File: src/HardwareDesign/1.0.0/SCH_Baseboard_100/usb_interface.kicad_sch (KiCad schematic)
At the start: 1 part, among them J3 USB-TYPE-C-018

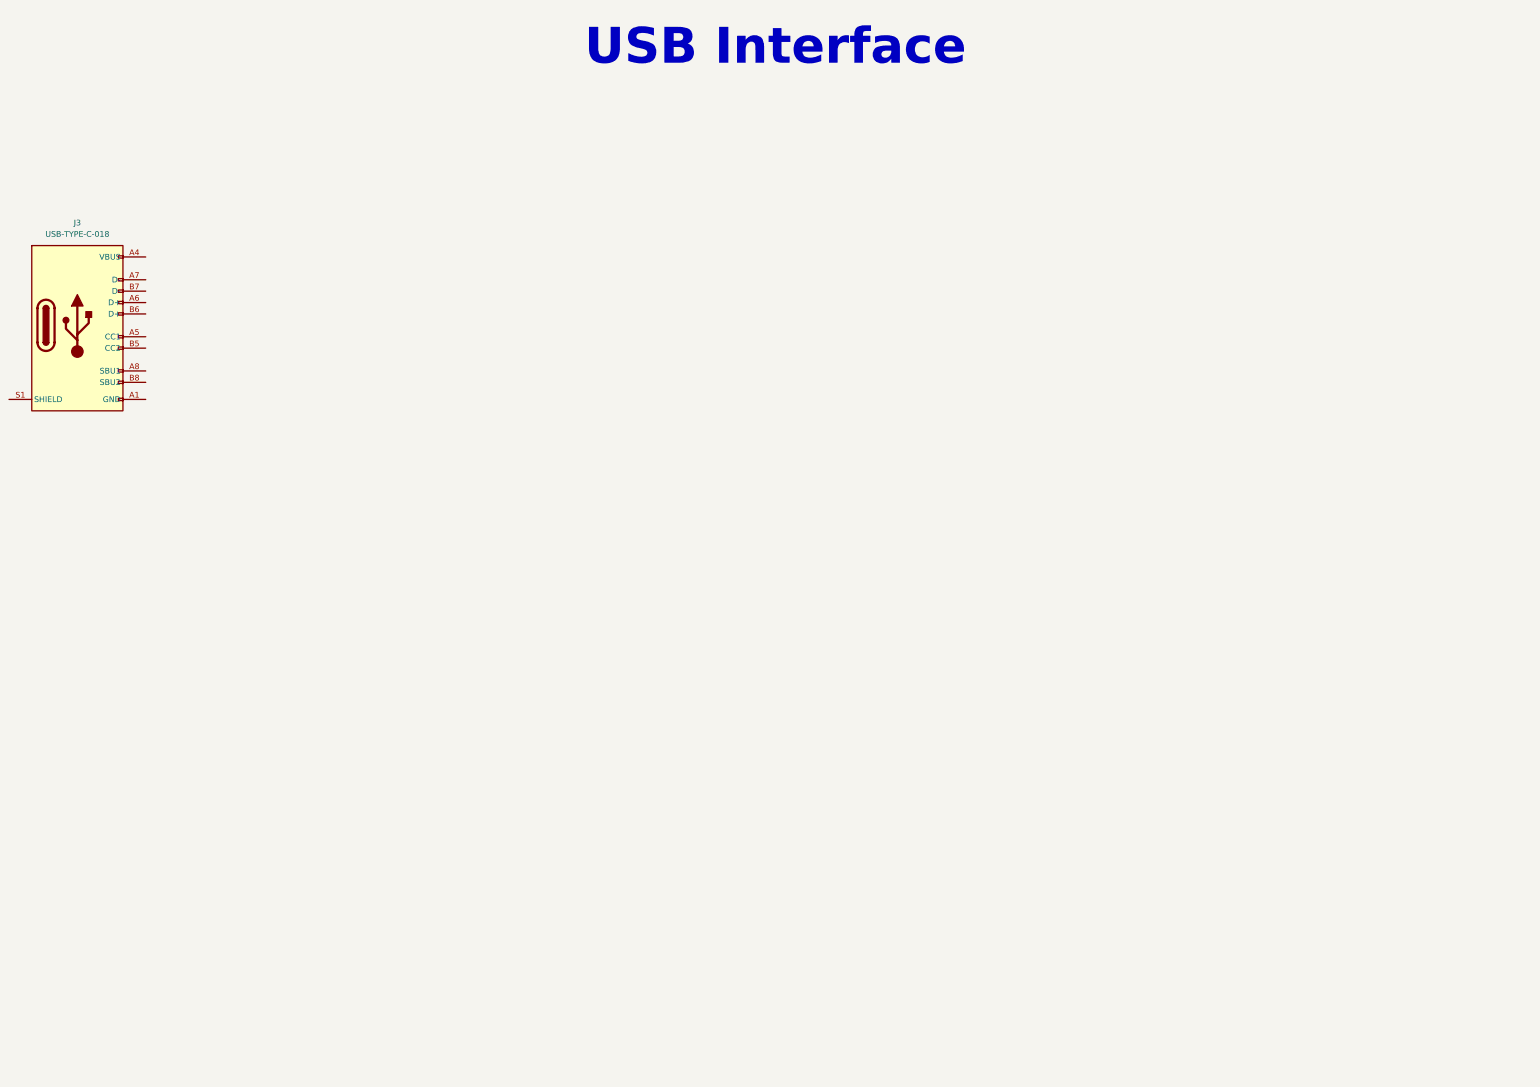
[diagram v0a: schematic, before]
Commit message: Add bladecore to design
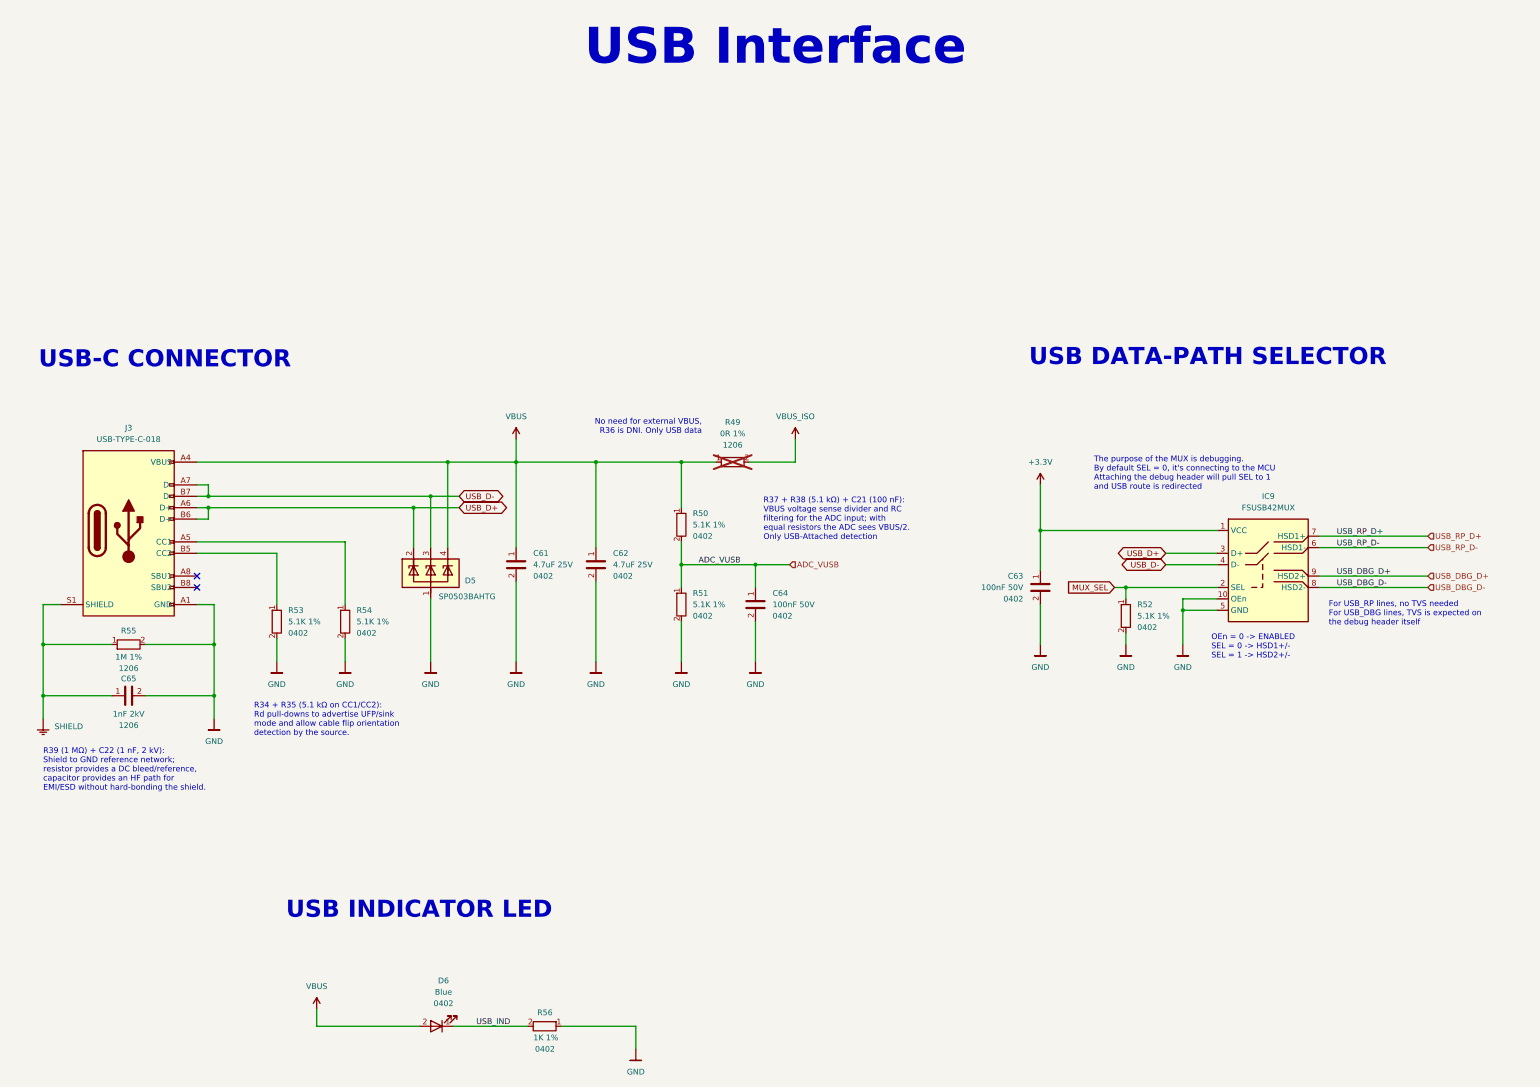
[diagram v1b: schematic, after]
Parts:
- added C61, C62: 4.7uF 25V, Capacitor_SMD:C_0402_1005Metric, symbol DS_Capacitor_0402:4.7uF 25V 0402
- added C63, C64: 100nF 50V, Capacitor_SMD:C_0402_1005Metric, symbol DS_Capacitor_0402:100nF 50V 0402
- added C65: 1nF 2kV, Capacitor_SMD:C_1206_3216Metric, symbol DS_Capacitor_1206:1nF 2kV 1206
- added D5: SP0503BAHTG, DS_Diode:SOT143, symbol DS_Diode:SP0503BAHTG
- added D6: Blue, LED_SMD:LED_0402_1005Metric, symbol DS_Opto:Blue 0402
- added IC9: FSUSB42MUX, DS_Peripherals:MSOP-10_3x3mm_P0.5mm, symbol DS_Peripherals:FSUSB42MUX
- added R49: 0R 1%, Resistor_SMD:R_1206_3216Metric, symbol DS_Resistor_1206:0R 1% 1206
- added R50, R51, R52, R53, R54: 5.1K 1%, Resistor_SMD:R_0402_1005Metric, symbol DS_Resistor_0402:5.1K 1% 0402
- added R55: 1M 1%, Resistor_SMD:R_1206_3216Metric, symbol DS_Resistor_1206:1M 1% 1206
- added R56: 1K 1%, Resistor_SMD:R_0402_1005Metric, symbol DS_Resistor_0402:1K 1% 0402
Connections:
- net GND: now reaches J3.A1 (GND), J3.A12 (GND), J3.B1 (GND), J3.B12 (GND)
- net GND: now also C61.2, C62.2, C63.2, C64.2, C65.2, D5.1, IC9.10 (OEn), IC9.5 (GND), R51.2, R52.2, R53.2, R54.2, R55.2, R56.1
- net VBUS: now reaches J3.A4 (VBUS), J3.A9 (VBUS), J3.B4 (VBUS), J3.B9 (VBUS)
- net VBUS: now also C61.1, C62.1, D5.4, D6.2, R49.1, R50.1
- net at J3.A5 (CC1): now also R54.1
- net USB_D+: now reaches J3.A6 (D+)
- net USB_D+: now also J3.B6 (D+), D5.2, IC9.3 (D+)
- net USB_D-: now reaches J3.A7 (D-)
- net USB_D-: now also J3.B7 (D-), D5.3, IC9.4 (D-)
- net at J3.B5 (CC2): now also R53.1
- net SHIELD: now reaches J3.S1 (SHIELD)
- net SHIELD: now also C65.1, R55.1
- new net +3.3V: C63.1, IC9.1 (VCC)
- new net ADC_VUSB: C64.1, R50.2, R51.1
- new net MUX_SEL: IC9.2 (SEL), R52.1
- new net USB_DBG_D+: IC9.9 (HSD2+)
- new net USB_DBG_D-: IC9.8 (HSD2-)
- new net USB_IND: D6.1, R56.2
- new net USB_RP_D+: IC9.7 (HSD1+)
- new net USB_RP_D-: IC9.6 (HSD1-)
- new net VBUS_ISO: R49.2
- no-connect marks 0 -> 2
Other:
- note added: "For USB_RP lines, no TVS needed For USB_DBG lines, TVS is expected on the debug header itself"
- note added: "No need for external VBUS, R36 is DNI. Only USB data"
- note added: "OEn = 0 -> ENABLED SEL = 0 -> HSD1+/- SEL = 1 -> HSD2+/-"
- note added: "R34 + R35 (5.1 kΩ on CC1/CC2): Rd pull-downs to advertise UFP/sink mode and allow cable flip orientation detection by the source."
- note added: "R37 + R38 (5.1 kΩ) + C21 (100 nF): VBUS voltage sense divider and RC filtering for the ADC input; with equal resistors the ADC sees VBUS/2. Only USB-Attached detection"
- note added: "R39 (1 MΩ) + C22 (1 nF, 2 kV): Shield to GND reference network; resistor provides a DC bleed/reference, capacitor provides an HF path for EMI/ESD without hard-bonding the shield."
- note added: "The purpose of the MUX is debugging. By default SEL = 0, it's connecting to the MCU Attaching the debug header will pull SEL to 1 and USB route is redirected"
- note added: "USB DATA-PATH SELECTOR"
- note added: "USB INDICATOR LED"
- note added: "USB-C CONNECTOR"
- moved on the sheet: J3
